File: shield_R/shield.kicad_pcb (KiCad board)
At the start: 2 copper layers, 85.1 x 78.7 mm, 15 parts, among them J3 Conn_01x01, J4 Conn_01x01, J5 Conn_01x01

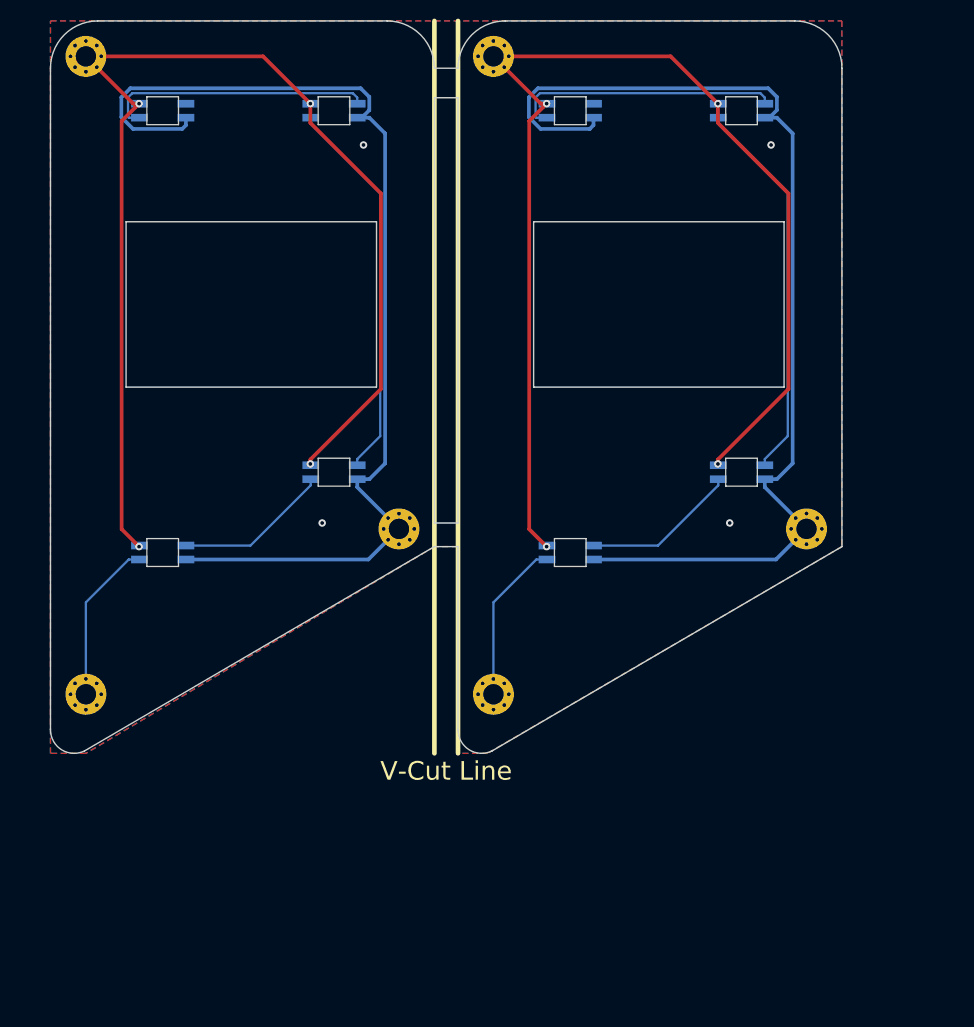
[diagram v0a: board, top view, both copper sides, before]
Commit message: change shelds v-cut
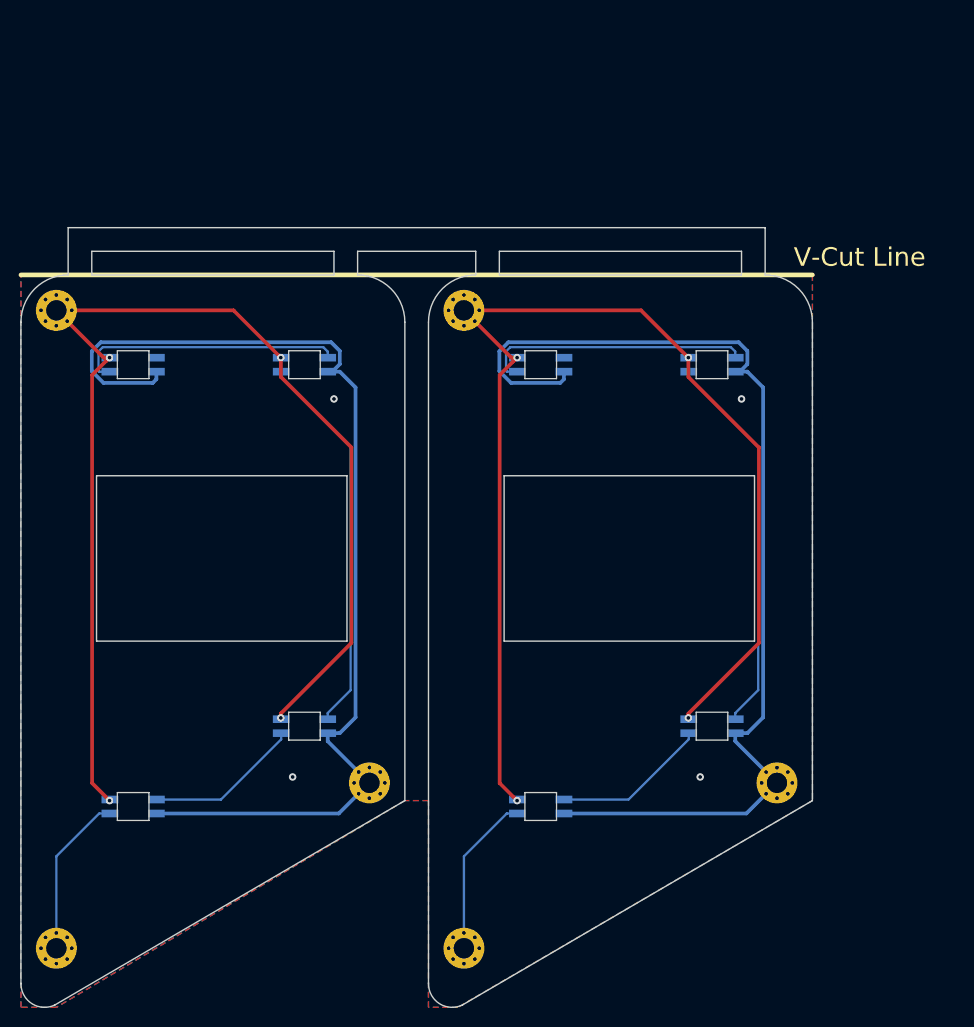
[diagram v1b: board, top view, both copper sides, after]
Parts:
- moved L1 27.5 mm to (161.9, 97.2)
- moved L1 27.5 mm to (118.1, 97.2)
- moved L2 27.5 mm to (180.3, 88.5)
- moved L2 27.5 mm to (136.5, 88.5)
- moved J5 27.5 mm to (109.9, 43.8)
- moved J5 27.5 mm to (153.7, 43.8)
- moved L3 27.5 mm to (180.3, 49.7)
- moved L3 27.5 mm to (136.5, 49.7)
- moved L4 27.5 mm to (161.9, 49.7)
- moved L4 27.5 mm to (118.1, 49.7)
- moved J3 27.5 mm to (153.7, 112.4)
- moved J3 27.5 mm to (109.9, 112.4)
- moved J4 27.5 mm to (143.5, 94.6)
- moved J4 27.5 mm to (187.3, 94.6)
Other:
- board size 85.1 x 78.7 mm -> 85.1 x 83.8 mm
